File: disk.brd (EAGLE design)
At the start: 40 x 40 mm, 0 parts

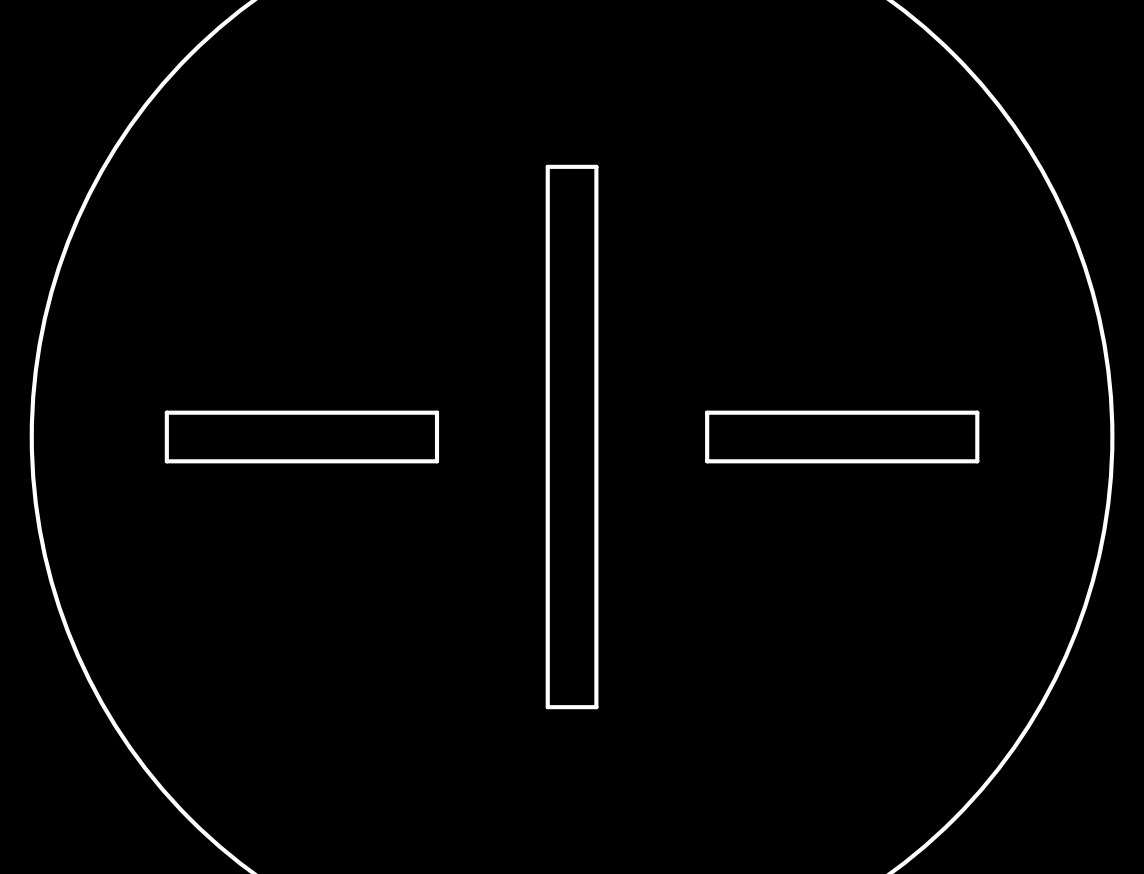
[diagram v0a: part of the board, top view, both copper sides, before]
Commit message: renamed circuits and fixed all dimensions
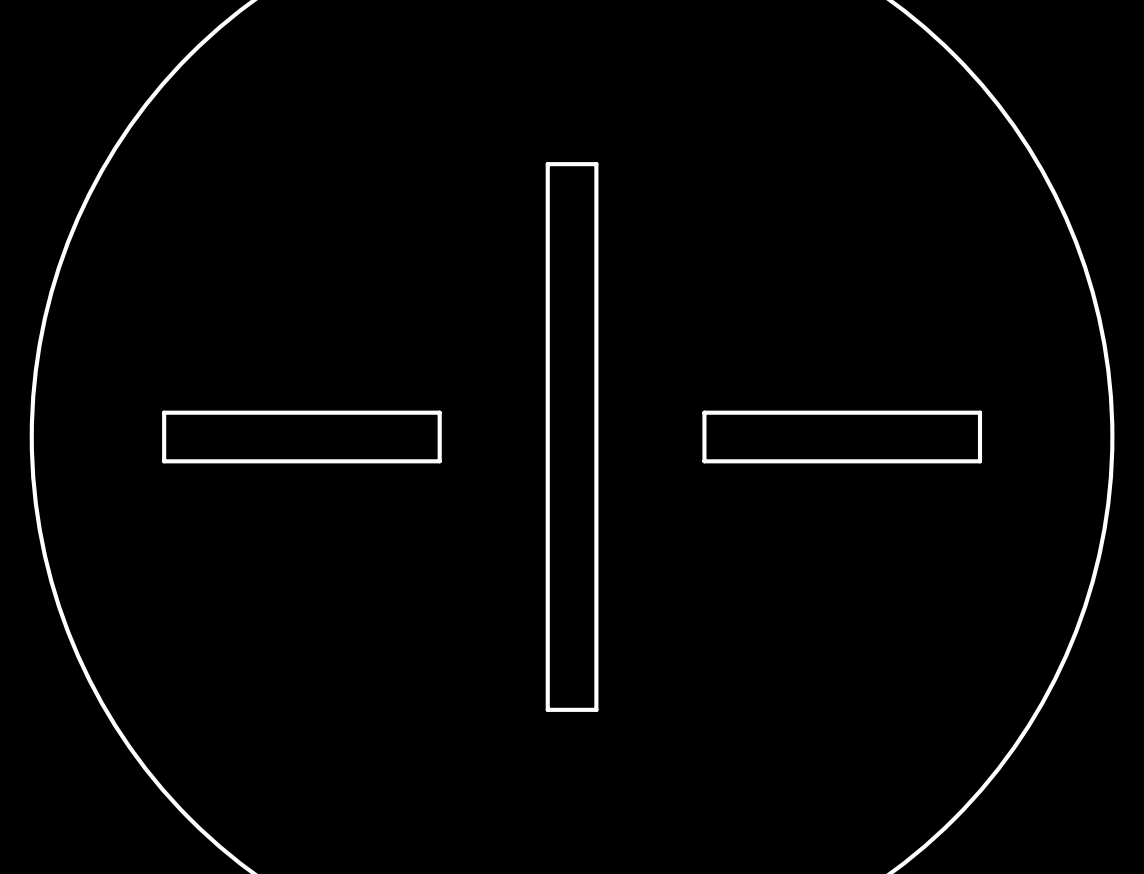
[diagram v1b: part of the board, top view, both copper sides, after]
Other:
- outline, holes or cut-outs redrawn
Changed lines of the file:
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@@
 <plain>
 <circle x="0" y="0" radius="20" width="0.1524" layer="20"/>
-<wire x1="-0.9" y1="10" x2="-0.9" y2="-10" width="0.1524" layer="20"/>
-<wire x1="-0.9" y1="-10" x2="0.9" y2="-10" width="0.1524" layer="20"/>
-<wire x1="0.9" y1="-10" x2="0.9" y2="10" width="0.1524" layer="20"/>
-<wire x1="0.9" y1="10" x2="-0.9" y2="10" width="0.1524" layer="20"/>
-<wire x1="5" y1="0.9" x2="5" y2="-0.9" width="0.1524" layer="20"/>
-<wire x1="5" y1="-0.9" x2="15" y2="-0.9" width="0.1524" layer="20"/>
-<wire x1="15" y1="-0.9" x2="15" y2="0.9" width="0.1524" layer="20"/>
-<wire x1="5" y1="0.9" x2="15" y2="0.9" width="0.1524" layer="20"/>
-<wire x1="-15" y1="0.9" x2="-5" y2="0.9" width="0.1524" layer="20"/>
-<wire x1="-5" y1="0.9" x2="-5" y2="-0.9" width="0.1524" layer="20"/>
-<wire x1="-5" y1="-0.9" x2="-15" y2="-0.9" width="0.1524" layer="20"/>
-<wire x1="-15" y1="-0.9" x2="-15" y2="0.9" width="0.1524" layer="20"/>
-<dimension x1="-0.8" y1="-10" x2="0.8" y2="-10" x3="0" y3="-12" textsize="1.778" layer="20"/>
-<dimension x1="-0.8" y1="10" x2="-0.8" y2="-10" x3="-2" y3="0" textsize="1.778" layer="20"/>
-<dimension x1="-5" y1="-0.8" x2="-15" y2="-0.8" x3="-10" y3="-4" textsize="1.778" layer="20"/>
-<dimension x1="-15" y1="-0.8" x2="-15" y2="0.8" x3="-16" y3="0" textsize="1.778" layer="20"/>
+<wire x1="-0.9" y1="10.1" x2="-0.9" y2="-10.1" width="0.1524" layer="20"/>
+<wire x1="-0.9" y1="-10.1" x2="0.9" y2="-10.1" width="0.1524" layer="20"/>
+<wire x1="0.9" y1="-10.1" x2="0.9" y2="10.1" width="0.1524" layer="20"/>
+<wire x1="0.9" y1="10.1" x2="-0.9" y2="10.1" width="0.1524" layer="20"/>
+<wire x1="4.9" y1="0.9" x2="4.9" y2="-0.9" width="0.1524" layer="20"/>
+<wire x1="4.9" y1="-0.9" x2="15.1" y2="-0.9" width="0.1524" layer="20"/>
+<wire x1="15.1" y1="-0.9" x2="15.1" y2="0.9" width="0.1524" layer="20"/>
+<wire x1="4.9" y1="0.9" x2="15.1" y2="0.9" width="0.1524" layer="20"/>
+<wire x1="-15.1" y1="0.9" x2="-4.9" y2="0.9" width="0.1524" layer="20"/>
+<wire x1="-4.9" y1="0.9" x2="-4.9" y2="-0.9" width="0.1524" layer="20"/>
+<wire x1="-4.9" y1="-0.9" x2="-15.1" y2="-0.9" width="0.1524" layer="20"/>
+<wire x1="-15.1" y1="-0.9" x2="-15.1" y2="0.9" width="0.1524" layer="20"/>
+<dimension x1="-15" y1="-0.9" x2="-15" y2="0.9" x3="-21" y3="0" textsize="1.778" layer="20"/>
+<dimension x1="15" y1="-0.9" x2="15" y2="0.9" x3="21" y3="0" textsize="1.778" layer="20"/>
+<dimension x1="-4.9" y1="-0.9" x2="-15.1" y2="-0.9" x3="-10" y3="-4" textsize="1.778" layer="20"/>
+<dimension x1="4.9" y1="-0.9" x2="15.1" y2="-0.9" x3="10" y3="-4" textsize="1.778" layer="20"/>
+<dimension x1="0.9" y1="-10.1" x2="0.9" y2="10.1" x3="-2" y3="0" textsize="1.778" layer="20"/>
+<dimension x1="0.9" y1="10.1" x2="-0.9" y2="10.1" x3="0" y3="11" textsize="1.778" layer="20"/>
+<dimension x1="0" y1="0" x2="4.9" y2="0" x3="2.45" y3="-12" textsize="1.778" layer="20"/>
+<dimension x1="15.1" y1="0" x2="20" y2="0" x3="17.55" y3="-9" textsize="1.778" layer="20"/>
+<dimension x1="0" y1="0" x2="16" y2="12" x3="8" y3="6" textsize="1.778" layer="20"/>
 </plain>
 <attributes>

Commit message: reworked boards and gerber files
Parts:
- added J1: 1X2-3.5MM, adafruit:1X2-3.5MM
- added LED1: (no value), adafruit:CHIPLED_0805
- added R1: (no value), adafruit:M0805
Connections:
- new net GND: J1.2, LED1.C
- new net N$1: J1.1, R1.2
- new net N$2: LED1.A, R1.1
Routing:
- net N$1: track 0.00 -> 17.9 mm
- net N$2: track 0.00 -> 3.12 mm
- net GND: track 0.00 -> 2.12 mm, vias 0 -> 1
- added copper zone on layer 16, net GND
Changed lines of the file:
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@@
 <layer number="45" name="Holes" color="7" fill="1" visible="yes" active="yes"/>
 <layer number="46" name="Milling" color="3" fill="1" visible="no" active="yes"/>
-<layer number="47" name="Measures" color="7" fill="1" visible="no" active="yes"/>
+<layer number="47" name="Measures" color="7" fill="1" visible="yes" active="yes"/>
 <layer number="48" name="Document" color="7" fill="1" visible="yes" active="yes"/>
 <layer number="49" name="Reference" color="7" fill="1" visible="yes" active="yes"/>
@@
 <board>
 <plain>
-<circle x="0" y="0" radius="20" width="0.1524" layer="20"/>
-<wire x1="-0.9" y1="10.1" x2="-0.9" y2="-10.1" width="0.1524" layer="20"/>
-<wire x1="-0.9" y1="-10.1" x2="0.9" y2="-10.1" width="0.1524" layer="20"/>
-<wire x1="0.9" y1="-10.1" x2="0.9" y2="10.1" width="0.1524" layer="20"/>
-<wire x1="0.9" y1="10.1" x2="-0.9" y2="10.1" width="0.1524" layer="20"/>
-<wire x1="4.9" y1="0.9" x2="4.9" y2="-0.9" width="0.1524" layer="20"/>
-<wire x1="4.9" y1="-0.9" x2="15.1" y2="-0.9" width="0.1524" layer="20"/>
-<wire x1="15.1" y1="-0.9" x2="15.1" y2="0.9" width="0.1524" layer="20"/>
-<wire x1="4.9" y1="0.9" x2="15.1" y2="0.9" width="0.1524" layer="20"/>
-<wire x1="-15.1" y1="0.9" x2="-4.9" y2="0.9" width="0.1524" layer="20"/>
-<wire x1="-4.9" y1="0.9" x2="-4.9" y2="-0.9" width="0.1524" layer="20"/>
-<wire x1="-4.9" y1="-0.9" x2="-15.1" y2="-0.9" width="0.1524" layer="20"/>
-<wire x1="-15.1" y1="-0.9" x2="-15.1" y2="0.9" width="0.1524" layer="20"/>
-<dimension x1="-15" y1="-0.9" x2="-15" y2="0.9" x3="-21" y3="0" textsize="1.778" layer="20"/>
-<dimension x1="15" y1="-0.9" x2="15" y2="0.9" x3="21" y3="0" textsize="1.778" layer="20"/>
-<dimension x1="-4.9" y1="-0.9" x2="-15.1" y2="-0.9" x3="-10" y3="-4" textsize="1.778" layer="20"/>
-<dimension x1="4.9" y1="-0.9" x2="15.1" y2="-0.9" x3="10" y3="-4" textsize="1.778" layer="20"/>
-<dimension x1="0.9" y1="-10.1" x2="0.9" y2="10.1" x3="-2" y3="0" textsize="1.778" layer="20"/>
-<dimension x1="0.9" y1="10.1" x2="-0.9" y2="10.1" x3="0" y3="11" textsize="1.778" layer="20"/>
-<dimension x1="0" y1="0" x2="4.9" y2="0" x3="2.45" y3="-12" textsize="1.778" layer="20"/>
-<dimension x1="15.1" y1="0" x2="20" y2="0" x3="17.55" y3="-9" textsize="1.778" layer="20"/>
-<dimension x1="0" y1="0" x2="16" y2="12" x3="8" y3="6" textsize="1.778" layer="20"/>
+<circle x="20" y="20" radius="20" width="0.1524" layer="20"/>
+<wire x1="19.1" y1="30.1" x2="19.1" y2="9.9" width="0.1524" layer="20"/>
+<wire x1="19.1" y1="9.9" x2="20.9" y2="9.9" width="0.1524" layer="20"/>
+<wire x1="20.9" y1="9.9" x2="20.9" y2="30.1" width="0.1524" layer="20"/>
+<wire x1="20.9" y1="30.1" x2="19.1" y2="30.1" width="0.1524" layer="20"/>
+<wire x1="24.9" y1="20.9" x2="24.9" y2="19.1" width="0.1524" layer="20"/>
+<wire x1="24.9" y1="19.1" x2="35.1" y2="19.1" width="0.1524" layer="20"/>
+<wire x1="35.1" y1="19.1" x2="35.1" y2="20.9" width="0.1524" layer="20"/>
+<wire x1="24.9" y1="20.9" x2="35.1" y2="20.9" width="0.1524" layer="20"/>
+<wire x1="4.9" y1="20.9" x2="15.1" y2="20.9" width="0.1524" layer="20"/>
+<wire x1="15.1" y1="20.9" x2="15.1" y2="19.1" width="0.1524" layer="20"/>
+<wire x1="15.1" y1="19.1" x2="4.9" y2="19.1" width="0.1524" layer="20"/>
+<wire x1="4.9" y1="19.1" x2="4.9" y2="20.9" width="0.1524" layer="20"/>
+<dimension x1="5" y1="19.1" x2="5" y2="20.9" x3="-1" y3="20" textsize="1.778" layer="47"/>
+<dimension x1="35" y1="19.1" x2="35" y2="20.9" x3="41" y3="20" textsize="1.778" layer="47"/>
+<dimension x1="15.1" y1="19.1" x2="4.9" y2="19.1" x3="10" y3="16" textsize="1.778" layer="47"/>
+<dimension x1="24.9" y1="19.1" x2="35.1" y2="19.1" x3="30" y3="16" textsize="1.778" layer="47"/>
+<dimension x1="20.9" y1="9.9" x2="20.9" y2="30.1" x3="18" y3="20" textsize="1.778" layer="47"/>
+<dimension x1="20.9" y1="30.1" x2="19.1" y2="30.1" x3="20" y3="31" textsize="1.778" layer="47"/>
+<dimension x1="20" y1="20" x2="24.9" y2="20" x3="22.45" y3="8" textsize="1.778" layer="47"/>
+<dimension x1="35.1" y1="20" x2="40" y2="20" x3="37.55" y3="11" textsize="1.778" layer="47"/>
+<dimension x1="20" y1="20" x2="36" y2="32" x3="28" y3="26" textsize="1.778" layer="47"/>
 </plain>
 <attributes>
@@
 <autorouter>
 <pass name="Default">
-<param name="RoutingGrid" value="50mil"/>
+<param name="RoutingGrid" value="6mil"/>
 <param name="AutoGrid" value="1"/>
 <param name="Efforts" value="0"/>
 <param name="TopRouterVariant" value="1"/>
 <param name="tpViaShape" value="round"/>
-<param name="PrefDir.1" value="a"/>
+<param name="PrefDir.1" value="*"/>
 <param name="PrefDir.2" value="0"/>
 <param name="PrefDir.3" value="0"/>
@@
 <param name="PrefDir.14" value="0"/>
 <param name="PrefDir.15" value="0"/>
-<param name="PrefDir.16" value="a"/>
-<param name="cfVia" value="8"/>
+<param name="PrefDir.16" value="*"/>
+<param name="cfVia" value="90"/>
 <param name="cfNonPref" value="5"/>
 <param name="cfChangeDir" value="2"/>
@@
 </pass>
 <pass name="Follow-me" refer="Default" active="yes">
+<param name="cfVia" value="8"/>
 </pass>
 <pass name="Busses" refer="Default" active="yes">
+<param name="cfVia" value="8"/>
 <param name="cfNonPref" value="4"/>
 <param name="cfBusImpact" value="4"/>
@@
 <pass name="Optimize1" refer="Default" active="yes">
 <param name="cfVia" value="99"/>
-<param name="cfExtdStep" value="10"/>
-<param name="cfHugging" value="1"/>
-<param name="mnExtdSteps" value="1"/>
-<param name="mnRipupLevel" value="0"/>
 </pass>
 <pass name="Optimize2" refer="Optimize1" active="yes">
-<param name="cfNonPref" value="0"/>
-<param name="cfChangeDir" value="6"/>
-<param name="cfExtdStep" value="0"/>
-<param name="cfBonusStep" value="2"/>
-<param name="cfMalusStep" value="2"/>
-<param name="cfPadImpact" value="2"/>
-<param name="cfSmdImpact" value="2"/>
-<param name="cfHugging" value="0"/>
 </pass>
 <pass name="Optimize3" refer="Optimize2" active="yes">
-<param name="cfChangeDir" value="8"/>
+<param name="cfBonusStep" value="0"/>
+<param name="cfMalusStep" value="0"/>
 <param name="cfPadImpact" value="0"/>
 <param name="cfSmdImpact" value="0"/>
+<param name="cfHugging" value="0"/>
 </pass>
 <pass name="Optimize4" refer="Optimize3" active="yes">
-<param name="cfChangeDir" value="25"/>
 </pass>
 </autorouter>
 <elements>
+<element name="J1" library="adafruit" library_urn="urn:adsk.eagle:library:420" package="1X2-3.5MM" package3d_urn="urn:adsk.eagle:package:6240635/1" value="1X2-3.5MM" x="11" y="27" smashed="yes">
+<attribute name="NAME" x="14" y="32" size="1.27" layer="25" rot="R180"/>
+</element>
+<element name="R1" library="adafruit" library_urn="urn:adsk.eagle:library:420" package="M0805" package3d_urn="urn:adsk.eagle:package:6240587/1" value="" x="13" y="11" smashed="yes" rot="R90">
+<attribute name="NAME" x="11.984" y="9.984" size="1.27" layer="25" rot="R90"/>
+<attribute name="VALUE" x="15.286" y="9.984" size="1.27" layer="27" rot="R90"/>
+</element>
+<element name="LED1" library="adafruit" library_urn="urn:adsk.eagle:library:420" package="CHIPLED_0805" package3d_urn="urn:adsk.eagle:package:6240559/1" value="" x="10" y="11" smashed="yes">
+<attribute name="NAME" x="8.73" y="9.73" size="1.27" layer="25" rot="R90"/>
+<attribute name="VALUE" x="12.54" y="9.73" size="1.27" layer="27" rot="R90"/>
+</element>
 </elements>
 <signals>
+<signal name="N$1">
+<contactref element="J1" pad="1"/>
+<contactref element="R1" pad="2"/>
+<wire x1="13.1064" y1="15.3924" x2="13.1064" y2="12.0396" width="0.1524" layer="1"/>
+<wire x1="16.3068" y1="18.5928" x2="13.1064" y2="15.3924" width="0.1524" layer="1"/>
+<wire x1="16.3068" y1="23.4696" x2="16.3068" y2="18.5928" width="0.1524" layer="1"/>
+<wire x1="12.8016" y1="26.9748" x2="16.3068" y2="23.4696" width="0.1524" layer="1"/>
+<wire x1="13.1064" y1="12.0396" x2="13" y2="11.95" width="0.1524" layer="1"/>
+<wire x1="12.8016" y1="26.9748" x2="12.8" y2="27" width="0.1524" layer="1"/>
+</signal>
+<signal name="N$2">
+<contactref element="R1" pad="1"/>
+<contactref element="LED1" pad="A"/>
+<wire x1="12.954" y1="9.906" x2="10.0584" y2="9.906" width="0.1524" layer="1"/>
+<wire x1="10.0584" y1="9.906" x2="10" y2="9.95" width="0.1524" layer="1"/>
+<wire x1="12.954" y1="9.906" x2="13" y2="10.05" width="0.1524" layer="1"/>
+</signal>
+<signal name="GND">
+<contactref element="LED1" pad="C"/>
+<contactref element="J1" pad="2"/>
+<polygon width="0.1524" layer="16">
+<vertex x="40" y="20" curve="180"/>
+<vertex x="0" y="20" curve="180"/>
+</polygon>
+<wire x1="9.906" y1="12.192" x2="10" y2="12.05" width="0.1524" layer="1"/>
+<via x="10" y="14" extent="1-16" drill="0.35"/>
+<wire x1="10" y1="12.05" x2="10" y2="14" width="0.1524" layer="1"/>
+</signal>
 </signals>
 <mfgpreviewcolors>
@@
 </board>
 </drawing>
+<compatibility>
+<note version="8.2" severity="warning">
+Since Version 8.2, EAGLE supports online libraries. The ids
+of those online libraries will not be understood (or retained)
+with this version.
+</note>
+<note version="8.3" severity="warning">
+Since Version 8.3, EAGLE supports URNs for individual library
+assets (packages, symbols, and devices). The URNs of those assets
+will not be understood (or retained) with this version.
+</note>
+<note version="8.3" severity="warning">
+Since Version 8.3, EAGLE supports the association of 3D packages
+with devices in libraries, schematics, and board files. Those 3D
+packages will not be understood (or retained) with this version.
+</note>
+</compatibility>
 </eagle>
